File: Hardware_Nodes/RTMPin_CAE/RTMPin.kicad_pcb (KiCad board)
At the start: 2 copper layers, 100 x 100 mm, 154 parts, among them J2 Conn_01x06, J3 Conn_01x06, J4 Conn_01x06, J5 Conn_01x06, J6 Conn_01x06, J7 Conn_01x06, J8 Conn_01x06, J9 Conn_01x06, Q2 IRLR3410, Q3 IRLR3410, Q4 IRLR3410, Q5 IRLR3410, Q6 IRLR3410, Q7 IRLR3410, Q8 IRLR3410, Q9 IRLR3410, U2 SN74LVC14A, U3 ADM3483, U4 BlackPill STM32F4xx, U5 SN74LVC14A, U6 SN74AHCT1G125, U7 SN74LVC14A

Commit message: HW bugfix
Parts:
- C1, C11, C12, C13, C14, C19, C2, C20, C21, C22, C23, C25, C26, C27, C3, C31, C33, C34, C35, C36, C37, C38, C39, C40, C7, C8, C9: footprint Capacitor_SMD:C_0603_1608Metric_Pad1.08x0.95mm_HandSolder -> Capacitor_SMD:C_0603_1608Metric
- C10, C15, C16, C17, C18, C28, C29, C30, C4, C5, C6: footprint Capacitor_SMD:C_1206_3216Metric_Pad1.33x1.80mm_HandSolder -> Capacitor_SMD:C_1206_3216Metric
- D10, D11, D15, D16, D17, D18, D19, D20, D24, D25, D27, D28, D29, D30, D5, D6, D7, D8, D9: footprint Diode_SMD:D_SOD-323_HandSoldering -> Diode_SMD:D_SOD-323
- R1, R10, R11, R12, R13, R14, R15, R16, R17, R18, R19, R2, R20, R21, R22, R23, R24, R25, R26, R27, R28, R29, R3, R30, R31, R32, R33, R35, R36, R37, R38, R39, R4, R40, R41, R42, R43, R44, R45, R46, R47, R48, R49, R5, R50, R51, R52, R53, R54, R55, R56, R57, R58, R6, R7, R8, R9: footprint Resistor_SMD:R_0603_1608Metric_Pad0.98x0.95mm_HandSolder -> Resistor_SMD:R_0603_1608Metric
- REF** (x4): value MountingHole_4.3mm_M4_DIN965 -> MountingHole_5.5mm_Pinball; footprint MountingHole:MountingHole_4.3mm_M4_DIN965 -> RTMPin_CAE:MountingHole_5.5mm_Pinball
- U6: footprint Package_TO_SOT_SMD:SOT-23-5_HandSoldering -> Package_TO_SOT_SMD:SOT-23-5
- moved R25 6.09 mm to (143.2, 47.2), turned to 0 degrees
- moved C24 3.72 mm to (135.8, 50.3)
- moved C10 3.31 mm to (116.5, 52.6), turned to 270 degrees
- moved TP3 2.96 mm to (112.3, 75.6)
- moved C3 2.03 mm to (109.5, 98.8)
- moved TP2 2.03 mm to (134.4, 67.1)
- moved U2 2.03 mm to (106.9, 105.4)
- moved U4 2.03 mm to (115.8, 56.9)
- moved C28 1.98 mm to (143.7, 45.0)
- moved R21 1.83 mm to (123.7, 52.0), turned to 0 degrees
- moved C20 1.52 mm to (144.4, 48.8)
- moved U6 1.52 mm to (143.9, 51.6)
- moved R6 0.80 mm to (118.9, 44.2)
- moved R8 0.80 mm to (123.6, 44.2)
- moved C11 0.80 mm to (119.5, 51.8)
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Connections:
- R21 pad 1: Net-(R21-Pad1) -> GND
- R21 pad 2: +3V3 -> Net-(R21-Pad2)
- U3 pad 2: Net-(R21-Pad1) -> Net-(R21-Pad2)
- U3 pad 3: Net-(R21-Pad1) -> Net-(R21-Pad2)
- U4 pad 6: Net-(U3-Pad1) -> Net-(U3-Pad4)
- U4 pad 7: Net-(U3-Pad4) -> Net-(U3-Pad1)
- U4 pad 9: Net-(R21-Pad1) -> Net-(R21-Pad2)
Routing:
- net Net-(R21-Pad1): track 50.4 -> 0.00 mm, vias 1 -> 0
- net Net-(R21-Pad2): track 0.00 -> 49.2 mm, vias 0 -> 1
- net +3V3: track 130.6 -> 126.4 mm
- net Net-(U3-Pad4): track 39.1 -> 35.2 mm
- net GND: track 152.4 -> 156.0 mm
- net /OB0: track 30.2 -> 26.6 mm
- net Net-(R25-Pad1): track 2.47 -> 5.55 mm
- net Net-(C14-Pad1): track 29.3 -> 31.8 mm
- net Net-(TP3-Pad1): track 6.25 -> 3.92 mm
- net Net-(C7-Pad1): track 13.5 -> 15.7 mm
- net Net-(C12-Pad1): track 12.2 -> 14.3 mm
- net /OA6: track 17.6 -> 15.5 mm
- net Net-(C9-Pad1): track 30.6 -> 32.6 mm
- net /OB8: track 50.2 -> 52.2 mm
- net /OB1: track 44.9 -> 46.9 mm
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
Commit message: HW bugfix
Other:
- board text added: "RTMPIN 0.1.1"
- board text removed: "RTMPIN 0.1"

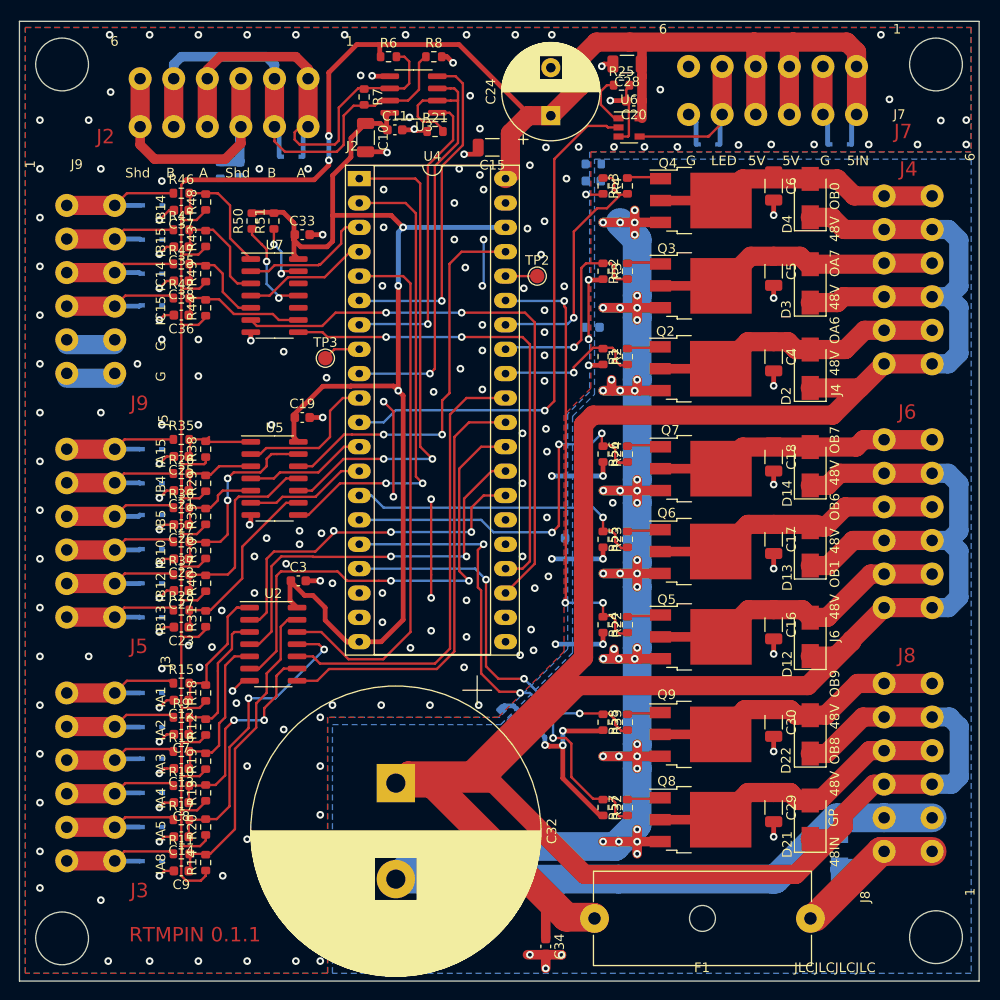
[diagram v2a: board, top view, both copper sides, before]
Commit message: all parts on top side
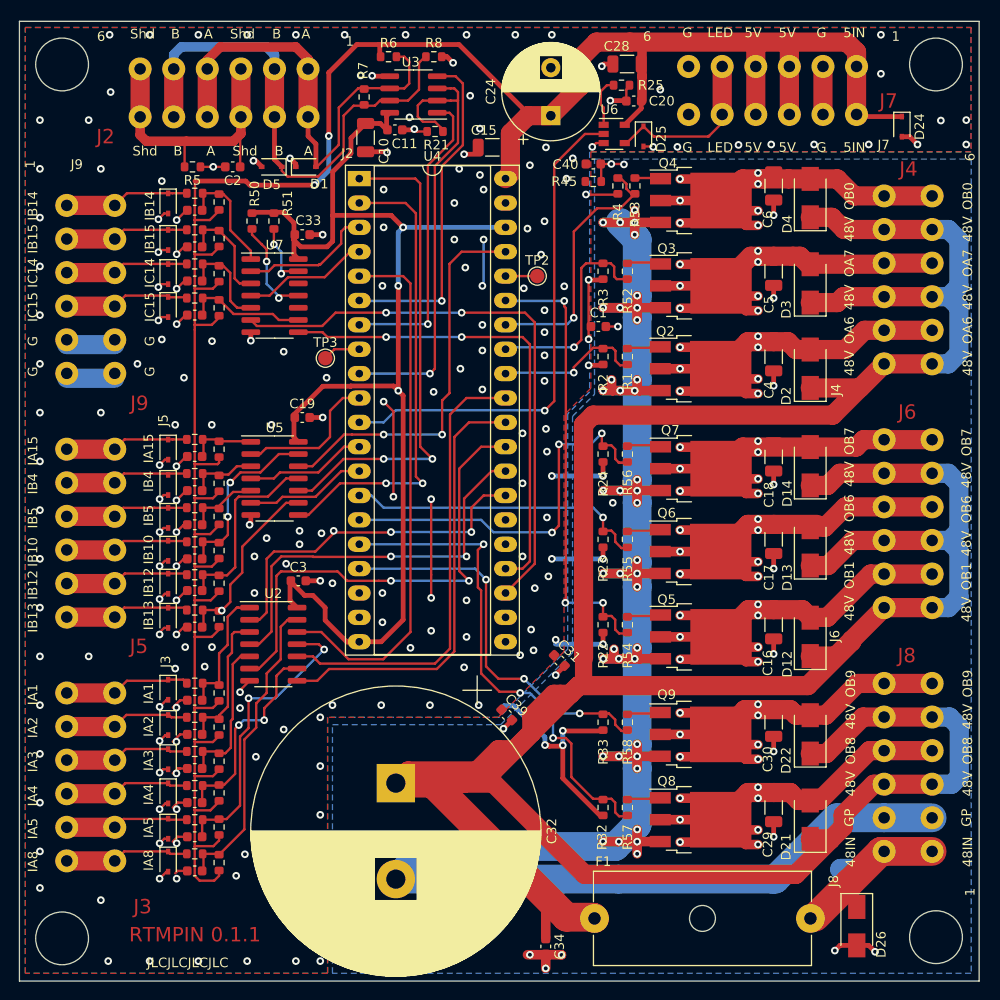
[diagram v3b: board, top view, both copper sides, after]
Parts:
- added D1: SD15C, Diode_SMD:D_SOD-323, F.Cu at (110.3, 55.7)
- C1, C2, C31, C39, C40, D10, D11, D15, D16, D17, D18, D19, D20, D24, D25, D26, D27, D28, D29, D30, D5, D6, D7, D8, D9, R45, R5: moved to F.Cu
- moved C31 12.8 mm to (136.7, 107.1), turned to 315 degrees
- moved D26 8.12 mm to (167.7, 134.8), turned to 270 degrees
- moved D25 6.78 mm to (145.4, 52.5), turned to 270 degrees
- moved D24 6.74 mm to (172.4, 51.5), turned to 270 degrees
- moved R5 2.92 mm to (98.4, 55.7), turned to 0 degrees
- moved D5 2.29 mm to (106.7, 55.7)
- moved R45 1.82 mm to (140.2, 57.2)
- moved C40 1.78 mm to (140.2, 55.4)
- moved D6 1.73 mm to (95.9, 110.2), turned to 270 degrees
- moved D17 1.72 mm to (95.9, 92.2), turned to 270 degrees
- moved D10 1.70 mm to (95.9, 124.6), turned to 270 degrees
- moved D16 1.70 mm to (95.9, 88.8), turned to 270 degrees
- moved D18 1.70 mm to (95.9, 95.7), turned to 270 degrees
- moved D20 1.69 mm to (95.9, 102.7), turned to 270 degrees
- moved D15 1.69 mm to (95.9, 85.1), turned to 270 degrees
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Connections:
- D5 pad 2: Net-(D5-Pad2) -> GND
- J2 pad 1: Net-(D5-Pad1) -> Net-(D1-Pad2)
- J2 pad 2: Net-(D5-Pad2) -> Net-(D5-Pad1)
- J2 pad 4: Net-(D5-Pad1) -> Net-(D1-Pad2)
- J2 pad 5: Net-(D5-Pad2) -> Net-(D5-Pad1)
- R6 pad 2: Net-(D5-Pad1) -> Net-(D1-Pad2)
- R7 pad 1: Net-(D5-Pad1) -> Net-(D1-Pad2)
- R7 pad 2: Net-(D5-Pad2) -> Net-(D5-Pad1)
- R8 pad 1: Net-(D5-Pad2) -> Net-(D5-Pad1)
- U3 pad 6: Net-(D5-Pad1) -> Net-(D1-Pad2)
- U3 pad 7: Net-(D5-Pad2) -> Net-(D5-Pad1)
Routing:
- net Net-(D5-Pad2): track 53.1 -> 0.00 mm
- net Net-(D1-Pad2): track 0.00 -> 50.1 mm
- net Net-(C29-Pad1): track 32.0 -> 51.7 mm, vias 0 -> 7
- net Net-(C16-Pad1): track 31.7 -> 51.4 mm, vias 0 -> 7
- net Net-(C4-Pad1): track 30.7 -> 50.3 mm, vias 0 -> 7
- net Net-(C17-Pad1): track 31.1 -> 50.7 mm, vias 0 -> 7
- net Net-(C30-Pad1): track 31.0 -> 50.7 mm, vias 0 -> 7
- net Net-(C5-Pad1): track 30.0 -> 49.6 mm, vias 0 -> 7
- net Net-(C6-Pad1): track 30.0 -> 49.7 mm, vias 0 -> 7
- net Net-(C18-Pad1): track 29.5 -> 49.2 mm, vias 0 -> 7
- net GND: track 156.0 -> 169.9 mm, vias 190 -> 205
- net GNDPWR: track 262.8 -> 275.7 mm, vias 52 -> 59
- net +5V: track 268.1 -> 256.5 mm
- net Net-(D5-Pad1): track 50.7 -> 55.1 mm
- net +48V: track 383.1 -> 386.0 mm
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
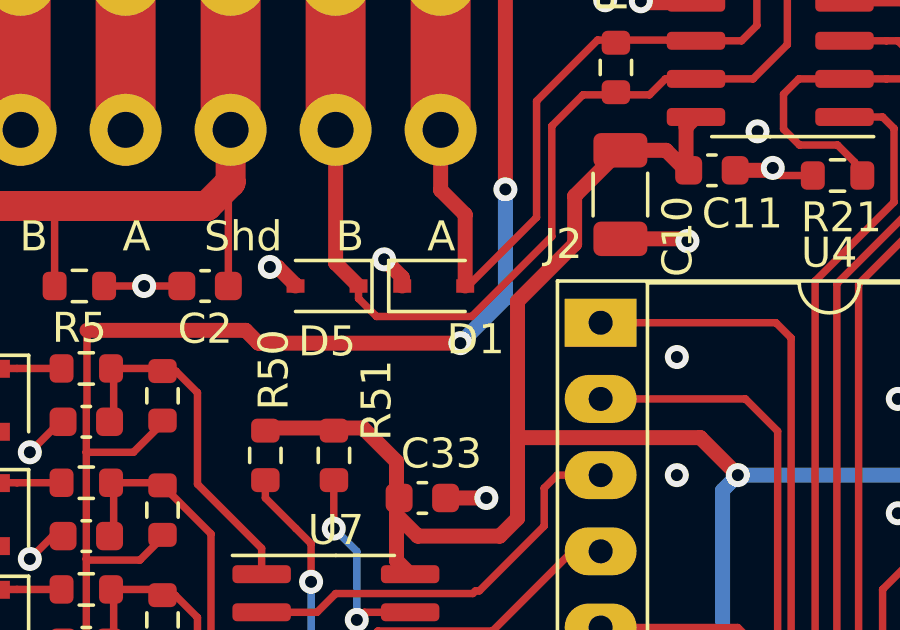
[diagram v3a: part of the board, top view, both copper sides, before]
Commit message: tvs unipolar
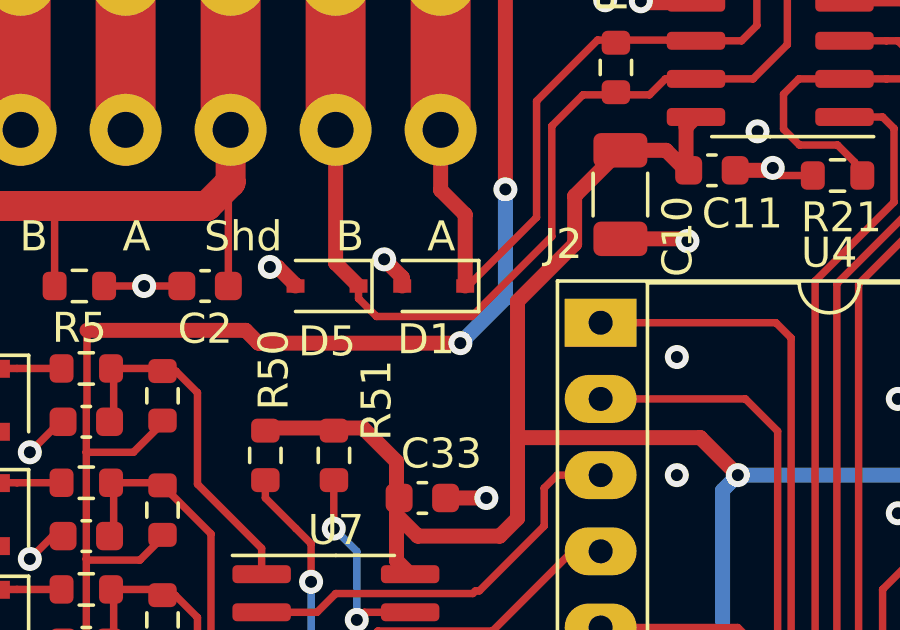
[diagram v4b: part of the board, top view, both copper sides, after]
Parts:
- C10: value 2u2 -> 10u 25V
- D1, D5: value SD15C -> SD15
- D10, D11, D15, D16, D17, D18, D19, D20, D24, D25, D27, D28, D29, D30, D6, D7, D8, D9: value SD15C -> SD05
- D26: value SMAJ48CA -> SMAJ48
- turned D1 to 180 degrees
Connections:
- D1 pad 1: GND -> Net-(D1-Pad1)
- D1 pad 2: Net-(D1-Pad2) -> GND
- J2 pad 1: Net-(D1-Pad2) -> Net-(D1-Pad1)
- J2 pad 4: Net-(D1-Pad2) -> Net-(D1-Pad1)
- R6 pad 2: Net-(D1-Pad2) -> Net-(D1-Pad1)
- R7 pad 1: Net-(D1-Pad2) -> Net-(D1-Pad1)
- U3 pad 6: Net-(D1-Pad2) -> Net-(D1-Pad1)
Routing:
- net Net-(D1-Pad2): track 50.1 -> 0.00 mm
- net Net-(D1-Pad1): track 0.00 -> 50.1 mm
